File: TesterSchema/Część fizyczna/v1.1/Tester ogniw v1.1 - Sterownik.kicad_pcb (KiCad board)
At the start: 2 copper layers, 82 parts, among them K1 D-SUB-DE-9, K2 JTAG-ATMEL, K3 K20, K4 K10, P2 500R, P3 1k, P4 100k, T1 BC547, T2 BC547, U1 TL082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

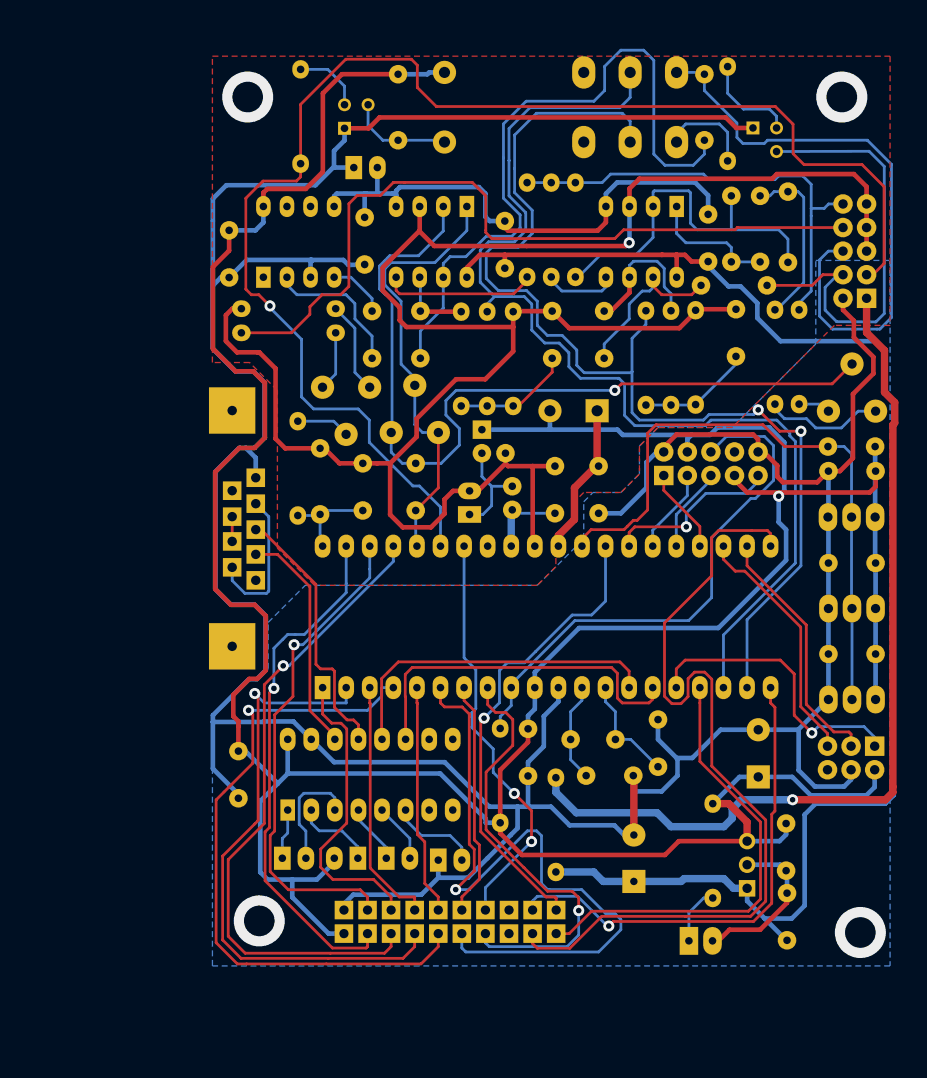
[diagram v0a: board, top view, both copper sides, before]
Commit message: Poprawa nazw warstw (naprawa błędu związanego z przejściem na nową wersję kicada)
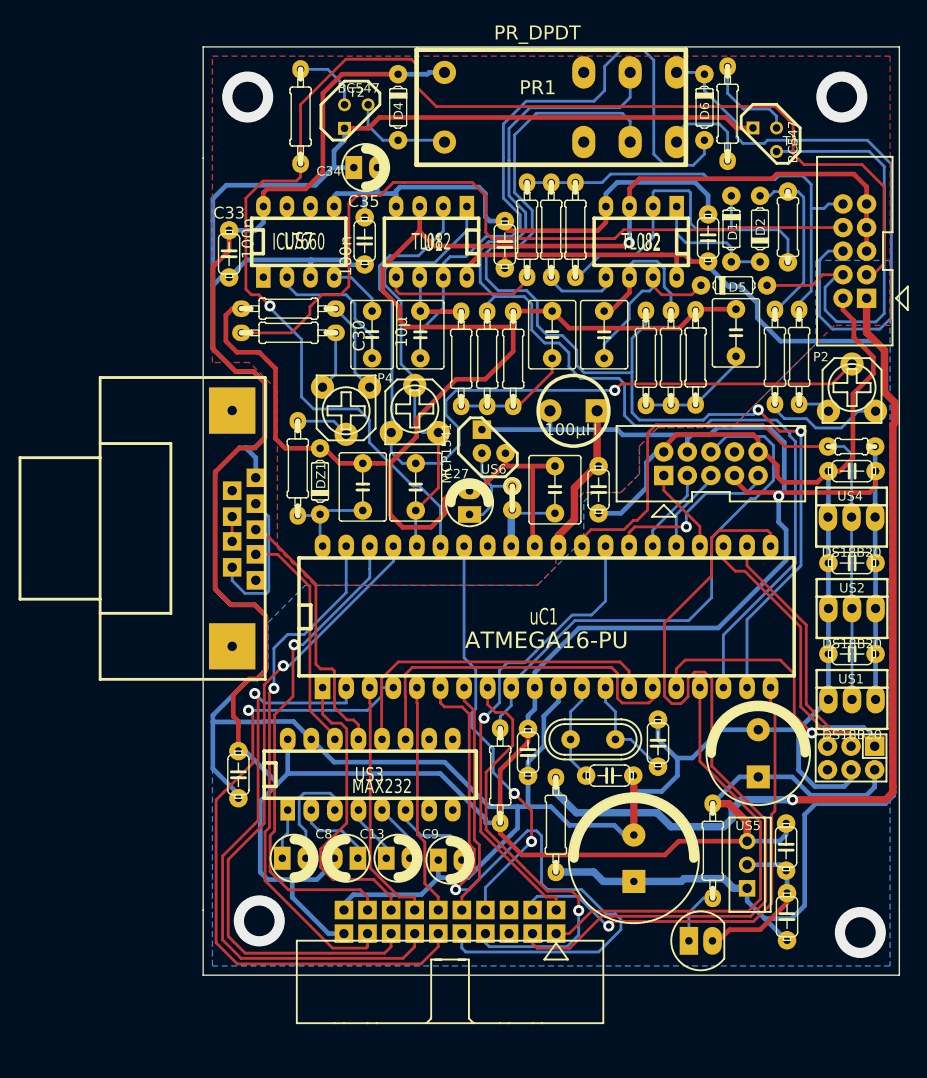
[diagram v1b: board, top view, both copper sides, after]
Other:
- board outline added: 75 x 100 mm

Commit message: Naprawa repo
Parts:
- R22: footprint resistor-0207/7 -> resistor-0207_7
- R28: footprint resistor-0207/2V -> resistor-0207_2V
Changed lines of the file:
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@@
     )
   )
-  (module resistor-0207/2V (layer Gorna)
+  (module resistor-0207_2V (layer Gorna)
     (at 144.5 96.2 270)
     (descr RESISTOR)
@@
     )
   )
-  (module resistor-0207/7 (layer Gorna)
+  (module resistor-0207_7 (layer Gorna)
     (at 174.2 67 90)
     (descr RESISTOR)
